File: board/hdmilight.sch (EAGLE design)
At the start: 73 parts, among them IC1 REG1117, IC2 REG1117, J1 POWER_JACKPTH, Q1 28.6363MHz

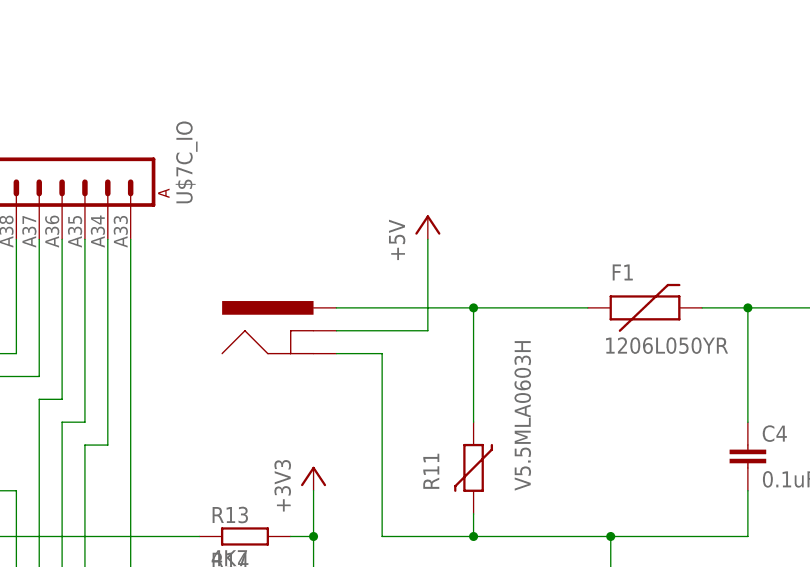
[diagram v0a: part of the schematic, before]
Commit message: fixed DC plug VCC/GND connection
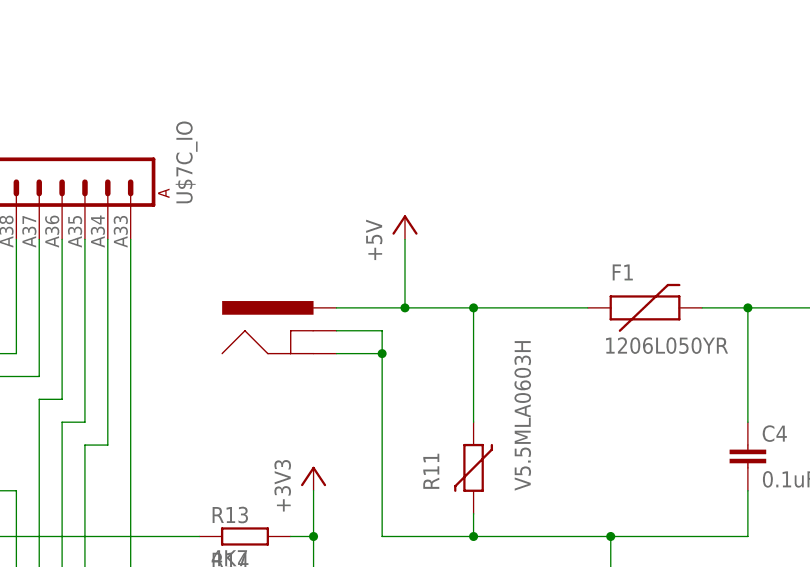
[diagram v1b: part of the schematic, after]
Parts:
- C1, C27, C28, C29, C30, C31, C32, C4: MF (none) -> AVX; MPN (none) -> 02016D104KAT2A; OC_FARNELL (none) -> 1657913
- C10, C11, C12, C13, C14, C9: MF (none) -> RUBYCON; MPN (none) -> 100ZLJ33M8X11.5; OC_FARNELL (none) -> 2102458
- C15, C18, C23, C25, C34, C36, C37: MF (none) -> AVX; MPN (none) -> 04025A150JAT2A; OC_FARNELL (none) -> 1327631
- C16, C17, C19, C20, C21, C22, C24, C26, C33, C35: MF (none) -> AVX; MPN (none) -> 06031A100JAT2A; OC_FARNELL (none) -> 1658863
- C2, C3: MF (none) -> AVX; MPN (none) -> 02013A470JAT2A; OC_FARNELL (none) -> 1657909RL
- C5, C6: MF (none) -> AVX; MPN (none) -> 06034D106MAT2A; OC_FARNELL (none) -> 1657928
- C7, C8: MF (none) -> AVX; MPN (none) -> 06034D226MAT2A; OC_FARNELL (none) -> 2094041RL
- F1: MF (none) -> LITTELFUSE; MPN (none) -> 1206L050YR; OC_FARNELL (none) -> 1596993
- IC1, IC2: MF (none) -> TEXAS INSTRUMENTS
- J1, L2, L3, L4, L5, L6, L7, LED1, LED2, R1, R10, R11, R12, R13, R14, R15, R2, R3, R4, R7, R8, U$1, U$2, U$3, U$4, U$5, U$6, U$7: OC_FARNELL (none) -> unknown
- R5: MF (none) -> AVX; MPN (none) -> 04025A100KAT2A; OC_FARNELL (none) -> 2332492RL
- R6: MF (none) -> MICROCHIP; MPN (none) -> 11AA010-I/P; OC_FARNELL (none) -> 1578282
- R9: MF (none) -> LABFACILITY; MPN (none) -> 010010TD; OC_FARNELL (none) -> 7255743
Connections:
- removed net N$17: F1.1, J1.PWR, R11.1
- net +5V: now also F1.1, J1.PWR, R11.1; no longer J1.GNDBREAK
- net GND: now also J1.GNDBREAK
